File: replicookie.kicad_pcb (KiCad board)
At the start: 4 copper layers, 152.4 x 114.3 mm, 160 parts, among them J1001 Conn_01x08_Female, J1002 Screw_Terminal_01x04, J1003 Conn_02x03_Odd_Even, J1004 Conn_01x08_Female, J1101 Conn_01x08_Female, J1102 Screw_Terminal_01x04, J1103 Conn_02x03_Odd_Even, J1104 Conn_01x08_Female, J1201 Conn_01x08_Female, J1202 Screw_Terminal_01x04, J1203 Conn_02x03_Odd_Even, J1204 Conn_01x08_Female, J1301 Conn_01x08_Female, J1302 Screw_Terminal_01x04, J1303 Conn_02x03_Odd_Even, J1304 Conn_01x08_Female, J1401 Conn_01x08_Female, J1402 Screw_Terminal_01x04, J1403 Conn_02x03_Odd_Even, J1404 Conn_01x08_Female, J1501 Conn_01x08_Female, J1502 Screw_Terminal_01x04, J1503 Conn_02x03_Odd_Even, J1504 Conn_01x08_Female, J301 USB_B_Micro, J401 JK0654219, J501 USB_A, J502 USB_A, J801 Conn_01x08_Female, J802 Screw_Terminal_01x04, J803 Conn_02x03_Odd_Even, J804 Conn_01x08_Female, J901 Conn_01x08_Female, J902 Screw_Terminal_01x04, J903 Conn_02x03_Odd_Even, J904 Conn_01x08_Female, P601 TFM-115-01-F-D-A, P602 TFM-120-01-F-D-A, U201 DS1307ZN+, U301 93LCxxBxxOT, U302 FT2232HQ, U401 MIC33050-4YHL, U402 TXS0102DCU, U403 KSZ9031RNXCA, U404 ASDMB-25.000MHz, U405 74LVC2G07, U501 ASDMB-24.000MHz-C, U502 ASDMB-26.000MHz-C, U503 USB3343, U504 74LVC1G07, U505 USB2514B_Bi, X201 ASE-xxxMHz, Y301 ABM8-12.000MHZ-20

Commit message: Connect Ethernet PHY to FPGA, route RGMII signals
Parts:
- removed the C402 at (113.0, 46.9)
- removed the C404 at (113.0, 48.9)
- removed the U402 at (144.8, 90.2)
- added C601: 0.1u, Capacitor_SMD:C_0603_1608Metric, F.Cu at (251.0, 116.3)
- added C602: 0.1u, Capacitor_SMD:C_0603_1608Metric, F.Cu at (255.0, 116.3)
- added U601: TCA9800, Package_SO:VSSOP-8_3.0x3.0mm_P0.65mm, F.Cu at (257.8, 106.0)
- C401: footprint Capacitor_SMD:C_0402_1005Metric -> Capacitor_SMD:C_0603_1608Metric; moved to F.Cu
- C402: renamed from C403; footprint Capacitor_SMD:C_0402_1005Metric -> Capacitor_SMD:C_0603_1608Metric; moved to F.Cu
- C403: renamed from C405; moved to F.Cu
- C408: renamed from C410; value 0.1U -> 0.1u; moved to B.Cu
- C409: renamed from C411; value 0.1U -> 0.1u; moved to B.Cu
- C410: renamed from C412; value 0.1U -> 0.1u
- C411: renamed from C413; value 0.1U -> 0.1u
- C412: renamed from C414; value 0.1U -> 0.1u
- C413: renamed from C415; value 0.1U -> 0.1u; moved to B.Cu
- C414: renamed from C416; value 0.1U -> 0.1u; moved to B.Cu
- C415: renamed from C417; value 0.1U -> 0.1u
- C416: renamed from C418; value 0.1U -> 0.1u; moved to B.Cu
- C417: renamed from C419; value 0.1U -> 0.1u
- C418: renamed from C420; value 0.1U -> 0.1u; moved to B.Cu
- C419: renamed from C421; value 0.1U -> 0.1u; moved to B.Cu
- C420: renamed from C422; value 0.1U -> 0.1u; moved to B.Cu
- C421: renamed from C423; value 0.1U -> 0.1u
- C422: renamed from C424; footprint Capacitor_SMD:C_0402_1005Metric -> Capacitor_SMD:C_0603_1608Metric
- C423: renamed from C425; footprint Capacitor_SMD:C_0402_1005Metric -> Capacitor_SMD:C_0603_1608Metric
- C425: renamed from C427; footprint Capacitor_SMD:C_0402_1005Metric -> Capacitor_SMD:C_0603_1608Metric
- C426: renamed from C428; footprint Capacitor_SMD:C_0402_1005Metric -> Capacitor_SMD:C_0603_1608Metric
- C427: renamed from C429; footprint Capacitor_SMD:C_0402_1005Metric -> Capacitor_SMD:C_0603_1608Metric
- C428: renamed from C430; footprint Capacitor_SMD:C_0402_1005Metric -> Capacitor_SMD:C_0603_1608Metric
- R403, R405: footprint Resistor_SMD:R_0603_1608Metric -> Resistor_SMD:R_0402_1005Metric; moved to B.Cu
- U401: moved to F.Cu
- U404: renamed from U405; moved to B.Cu
- moved C423 216.6 mm to (275.3, 124.7), turned to 180 degrees
- moved D401 199.6 mm to (272.2, 119.8), turned to -90 degrees
- moved R407 198.4 mm to (278.0, 127.1)
- moved D402 198.0 mm to (275.3, 126.6)
- moved U404 195.1 mm to (260.8, 124.3), turned to 90 degrees
- moved R403 181.4 mm to (255.9, 128.4), turned to 180 degrees
- moved R405 180.0 mm to (255.9, 126.7), turned to 180 degrees
- moved C403 175.9 mm to (284.5, 124.5), turned to -90 degrees
- moved C404 175.6 mm to (292.2, 133.8)
- moved C406 175.6 mm to (292.2, 135.7)
- moved C407 175.6 mm to (292.2, 137.6)
- moved C424 175.6 mm to (292.2, 139.5)
- moved FB401 175.6 mm to (288.4, 135.7)
- moved FB402 175.6 mm to (288.4, 137.6)
- moved FB403 175.6 mm to (288.4, 139.5)
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- renumbered C406 to C404, C407 to C405, C408 to C406, C409 to C407, C426 to C424, P601 to J2, P602 to J3, PA601 to JA1, PA602 to JA2, PB601 to JB1, PB602 to JB2, PC601 to JC1, U403 to U402, U404 to U403
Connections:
- net /Snickerdoodle/~ETHERNET_RST renamed Net-(J3-Pad2)
- net /Snickerdoodle/~USB_RST renamed Net-(J3-Pad4)
- net /ZYNQ_I2C1.SCL renamed /SMB_I2C1.SCL
- net /ZYNQ_I2C1.SDA renamed /SMB_I2C1.SDA
- net /ZYNQ_I2C2.SCL renamed /SMB_I2C2.SCL
- net /ZYNQ_I2C2.SDA renamed /SMB_I2C2.SDA
- net /ZYNQ_I2C3.SCL renamed /SMB_I2C3.SCL
- net /ZYNQ_I2C3.SDA renamed /SMB_I2C3.SDA
- net /ZYNQ_I2C4.SCL renamed /SMB_I2C4.SCL
- net /ZYNQ_I2C4.SDA renamed /SMB_I2C4.SDA
- net /ZYNQ_I2C5.SCL renamed /SMB_I2C5.SCL
- net /ZYNQ_I2C5.SDA renamed /SMB_I2C5.SDA
- net /ZYNQ_I2C7.SCL renamed /SMB_I2C7.SCL
- net /ZYNQ_I2C7.SDA renamed /SMB_I2C7.SDA
- net /~RESET renamed /~USB_RST
- net Net-(C327-Pad1) renamed /Ethernet/CT4
- net Net-(C328-Pad1) renamed /Ethernet/CT3
- net Net-(C329-Pad1) renamed /Ethernet/CT2
- net Net-(C330-Pad1) renamed /Ethernet/CT1
- net Net-(J301-Pad14) renamed /Ethernet/LED2A
- net Net-(J301-Pad16) renamed /Ethernet/LED1A
- net Net-(R301-Pad2) renamed /Ethernet/LED_MODE
- net Net-(R306-Pad1) renamed /Ethernet/ISET
- C405 pad 1: +1V8 -> +3V3
- C408 pad 1: +1V8 -> +3V3
- C409 pad 1: +1V8 -> +3V3
- C410 pad 1: +1V8 -> +3V3
- D401 pad 1: +1V8 -> +3V3
- D402 pad 1: /~RESET_1 -> /~ETHERNET_RST
- J3 pad 11: /ETHERNET.TXD3 -> Net-(J3-Pad11)
- J3 pad 12: /ETHERNET.RXD0 -> Net-(J3-Pad12)
- J3 pad 13: /ETHERNET.TX_CTL -> Net-(J3-Pad13)
- J3 pad 14: /ETHERNET.RX_CLK -> Net-(J3-Pad14)
- J3 pad 17: /ETHERNET.RXD1 -> Net-(J3-Pad17)
- J3 pad 18: /ETHERNET.RX_CTL -> Net-(J3-Pad18)
- J3 pad 19: /ETHERNET.RXD2 -> Net-(J3-Pad19)
- J3 pad 20: /ETHERNET.RXD3 -> Net-(J3-Pad20)
- J3 pad 5: /ETHERNET.TX_CLK -> Net-(J3-Pad5)
- J3 pad 6: /ETHERNET.TXD2 -> /Snickerdoodle/SCK
- J3 pad 7: /ETHERNET.TXD0 -> Net-(J3-Pad7)
- J3 pad 8: /ETHERNET.TXD1 -> /Snickerdoodle/SCL
- JA2 pad 12: Net-(PA502-Pad12) -> /ETHERNET.TXD3
- JA2 pad 14: Net-(PA502-Pad14) -> /ETHERNET.TX_CLK
- JA2 pad 17: Net-(PA502-Pad17) -> /ETHERNET.MDIO
- JA2 pad 18: Net-(PA502-Pad18) -> /ETHERNET.TX_CTL
- JA2 pad 19: Net-(PA502-Pad19) -> /ETHERNET.MDC
- JA2 pad 20: Net-(PA502-Pad20) -> /ETHERNET.RXD3
- JA2 pad 24: Net-(PA502-Pad24) -> /ETHERNET.RXD2
- JA2 pad 26: Net-(PA502-Pad26) -> /ETHERNET.RXD1
- JA2 pad 30: Net-(PA502-Pad30) -> /ETHERNET.RXD0
- JA2 pad 32: Net-(PA502-Pad32) -> /ETHERNET.RX_CTL
- JA2 pad 36: /ETHERNET.MDC -> /ETHERNET.RX_CLK
- JA2 pad 38: /ETHERNET.MDIO -> /~ETHERNET_RST
- JA2 pad 4: Net-(PA502-Pad4) -> /ETHERNET.TXD0
- JA2 pad 6: Net-(PA502-Pad6) -> /ETHERNET.TXD1
- JA2 pad 8: Net-(PA502-Pad8) -> /ETHERNET.TXD2
- R401 pad 1: +1V8 -> +3V3
- R402 pad 1: +1V8 -> +3V3
- R402 pad 2: /Ethernet/LED2 -> /Ethernet/~INT~/~PME2
- R404 pad 1: +1V8 -> +3V3
- R404 pad 2: /Ethernet/MDIO -> /ETHERNET.MDIO
- R407 pad 1: +1V8 -> +3V3
- U402 pad 16: +1V8 -> +3V3
- U402 pad 34: +1V8 -> +3V3
- U402 pad 36: /Ethernet/MDC -> /ETHERNET.MDC
- U402 pad 37: /Ethernet/MDIO -> /ETHERNET.MDIO
- U402 pad 38: /Ethernet/LED2 -> /Ethernet/~INT~/~PME2
- U402 pad 40: +1V8 -> +3V3
- U404 pad 1: /Ethernet/LED1 -> /Ethernet/LED2
- U404 pad 3: /Ethernet/LED2 -> /Ethernet/LED1
- U404 pad 4: /Ethernet/LED2K -> /Ethernet/LED1K
- U404 pad 5: +1V8 -> +3V3
- U404 pad 6: /Ethernet/LED1K -> /Ethernet/LED2K
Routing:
- net /ETHERNET.TX_CTL: track 0.00 -> 42.0 mm
- net /ETHERNET.TXD3: track 0.00 -> 42.0 mm
- net /ETHERNET.TX_CLK: track 0.00 -> 41.9 mm
- net /ETHERNET.TXD0: track 0.00 -> 41.9 mm
- net /ETHERNET.TXD1: track 0.00 -> 41.8 mm
- net /ETHERNET.TXD2: track 0.00 -> 41.7 mm
- net /ETHERNET.RX_CLK: track 0.00 -> 33.2 mm
- net /ETHERNET.RXD1: track 0.00 -> 33.1 mm
- net /ETHERNET.RX_CTL: track 0.00 -> 33.0 mm
- net /ETHERNET.RXD2: track 0.00 -> 33.0 mm
- net /ETHERNET.RXD3: track 0.00 -> 32.7 mm
- net /ETHERNET.RXD0: track 0.00 -> 32.5 mm
- net GND: track 0.00 -> 23.7 mm, vias 0 -> 4
- net /Ethernet/LED1: track 0.00 -> 9.27 mm, vias 0 -> 1
- net /Ethernet/DVDDL: track 16.8 -> 24.7 mm, vias 0 -> 6
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- added copper zone on In2.Cu, net +3V3
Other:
- board size 152.4 x 114.3 mm -> 160 x 120 mm

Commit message: Attach ethernet to PL, layout and route
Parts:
- added C429: 0.1u, Capacitor_SMD:C_0603_1608Metric, F.Cu at (260.2, 121.0)
- C401, C403, C404, C405, C406, C407, C415, C421, U401: moved to B.Cu
- C402: footprint Capacitor_SMD:C_0603_1608Metric -> Capacitor_SMD:C_0402_1005Metric; moved to B.Cu
- D401, D402: value 1N4148WS -> 1N4148WT; footprint Diode_SMD:D_SOD-323 -> Diode_SMD:D_SOD-523
- FB301, FB302: footprint Inductor_SMD:L_0603_1608Metric -> Inductor_SMD:L_0402_1005Metric
- FB401, FB402, FB403: footprint Inductor_SMD:L_0603_1608Metric -> Inductor_SMD:L_0402_1005Metric; moved to B.Cu
- R401: footprint Resistor_SMD:R_0603_1608Metric -> Resistor_SMD:R_0402_1005Metric; moved to B.Cu
- R402, R404, R406: footprint Resistor_SMD:R_0603_1608Metric -> Resistor_SMD:R_0402_1005Metric
- R403, R405, U404: moved to F.Cu
- U302: value FT2232HQ -> FT4232H; footprint Package_DFN_QFN:QFN-64-1EP_9x9mm_P0.5mm_EP4.35x4.35mm -> Package_QFP:LQFP-64_10x10mm_P0.5mm
- moved C427 110.8 mm to (285.0, 115.0), turned to -90 degrees
- moved R404 101.4 mm to (279.5, 134.8), turned to 180 degrees
- moved U302 89.8 mm to (158.5, 91.2)
- moved R408 78.1 mm to (269.5, 115.0), turned to -90 degrees
- moved C422 75.8 mm to (282.5, 125.0), turned to 180 degrees
- moved C425 74.1 mm to (263.5, 115.0), turned to -90 degrees
- moved U403 72.6 mm to (282.5, 128.0), turned to 180 degrees
- moved R402 69.6 mm to (279.5, 133.5), turned to 180 degrees
- moved R401 66.1 mm to (278.8, 131.5), turned to 180 degrees
- moved R406 65.7 mm to (279.0, 128.0)
- moved R409 59.3 mm to (280.0, 115.0), turned to -90 degrees
- moved C428 59.0 mm to (282.5, 115.0), turned to -90 degrees
- moved C426 42.5 mm to (261.0, 115.0), turned to -90 degrees
- moved U401 41.8 mm to (287.7, 134.8), turned to 180 degrees
- moved C424 28.1 mm to (268.0, 125.2), turned to 90 degrees
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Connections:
- net /Ethernet/~RESET_IN renamed /Ethernet/~ENET_RST
- net /SCL renamed /SMB_I2C0.SCL
- net /SDA renamed /SMB_I2C0.SDA
- net Net-(U504-Pad4) renamed /USB/~HUB_RESET
- C422 pad 2: Net-(C422-Pad2) -> GND
- J401 pad 4: /Ethernet/TXRXB+ -> /Ethernet/TXRXB-
- J401 pad 5: /Ethernet/TXRXB- -> /Ethernet/TXRXB+
- J401 pad 8: /Ethernet/TXRXD+ -> /Ethernet/TXRXD-
- J401 pad 9: /Ethernet/TXRXD- -> /Ethernet/TXRXD+
- JA2 pad 17: /ETHERNET.MDIO -> Net-(JA2-Pad17)
- JA2 pad 19: /ETHERNET.MDC -> Net-(JA2-Pad19)
- JA2 pad 31: Net-(JA2-Pad31) -> /~ETHERNET_RST
- JA2 pad 35: Net-(JA2-Pad35) -> /ETHERNET.MDIO
- JA2 pad 37: Net-(JA2-Pad37) -> /ETHERNET.MDC
- JA2 pad 38: /~ETHERNET_RST -> Net-(JA2-Pad38)
- U403 pad 2: Net-(C422-Pad2) -> GND
- U404 pad 1: /Ethernet/LED2 -> /Ethernet/LED1
- U404 pad 3: /Ethernet/LED1 -> /Ethernet/LED2
- U404 pad 4: /Ethernet/LED1K -> /Ethernet/LED2K
- U404 pad 6: /Ethernet/LED2K -> /Ethernet/LED1K
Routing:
- net /~ETHERNET_RST: track 0.00 -> 42.3 mm
- net /ETHERNET.MDIO: track 0.00 -> 38.5 mm
- net /ETHERNET.MDC: track 0.00 -> 35.6 mm
- net +3V3: track 7.11 -> 30.8 mm, vias 3 -> 11
- net /Ethernet/TXRXB+: track 0.00 -> 23.4 mm
- net /Ethernet/TXRXC-: track 0.00 -> 23.4 mm
- net /Ethernet/TXRXB-: track 0.00 -> 22.6 mm
- net /Ethernet/TXRXC+: track 0.00 -> 22.6 mm
- net /Ethernet/TXRXA+: track 0.00 -> 20.6 mm
- net /Ethernet/TXRXD-: track 0.00 -> 20.6 mm
- net /Ethernet/TXRXA-: track 0.00 -> 19.9 mm
- net /Ethernet/TXRXD+: track 0.00 -> 19.9 mm
- net /Ethernet/LED1K: track 0.00 -> 19.9 mm, vias 0 -> 1
- net /Ethernet/CT2: track 0.00 -> 12.7 mm
- net /Ethernet/CT3: track 0.00 -> 12.5 mm
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- added copper zone on B.Cu, net +3V3
- added copper zone on B.Cu, net /Ethernet/DVDDL
- added copper zone on In2.Cu, net /Ethernet/DVDDL
- added copper zone on B.Cu, net Net-(U401-Pad3)

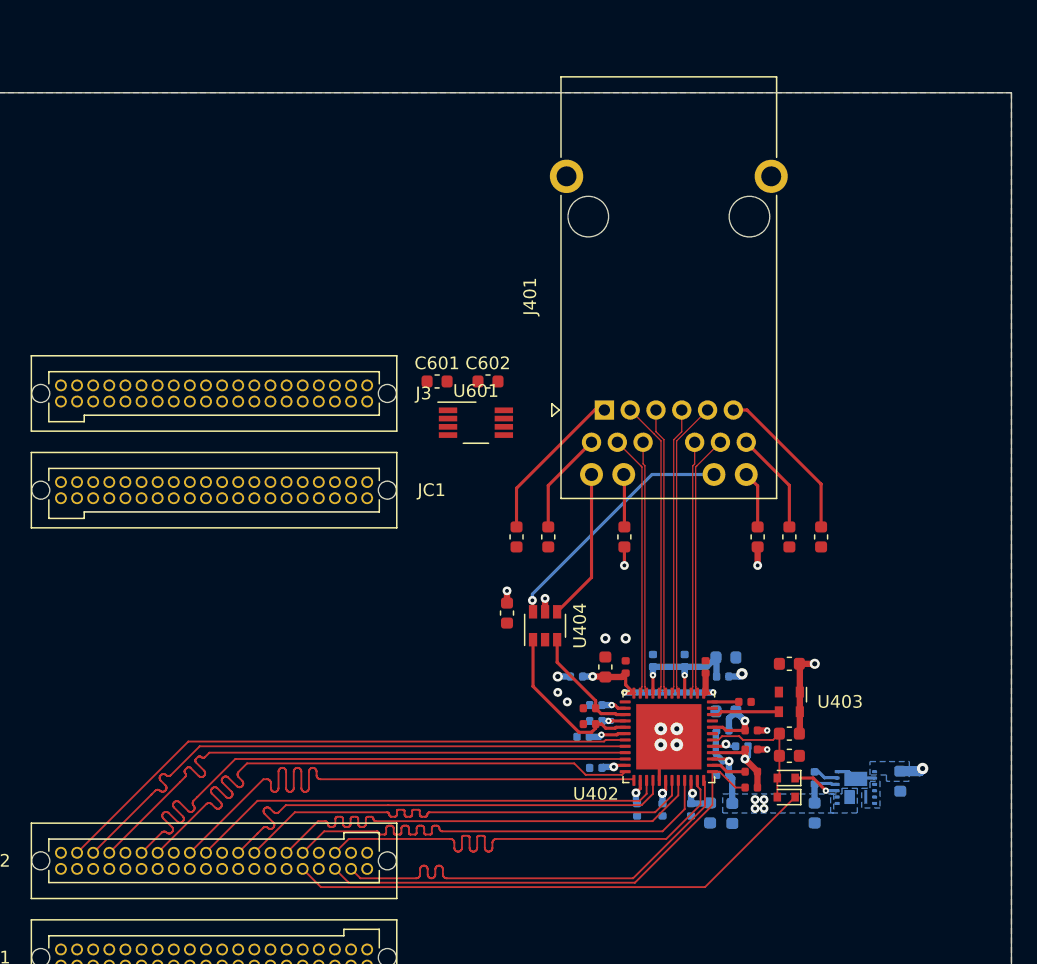
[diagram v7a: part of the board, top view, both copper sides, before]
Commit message: Move Ethernet around to save space
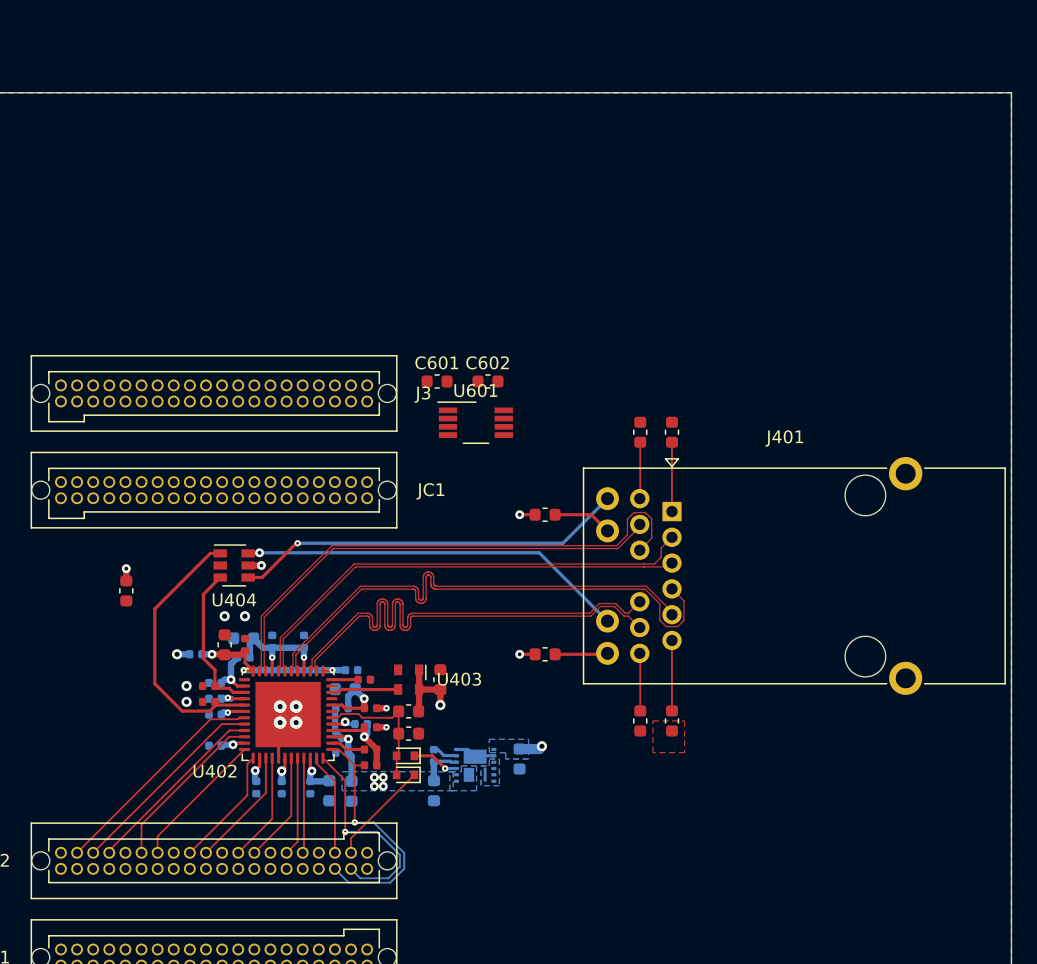
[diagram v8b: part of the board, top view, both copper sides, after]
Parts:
- C411: moved to B.Cu
- moved C406 38.0 mm to (239.5, 123.0), turned to 180 degrees
- moved FB401 37.8 mm to (239.5, 124.5), turned to 180 degrees
- moved C412 30.1 mm to (239.6, 123.5)
- moved FB403 30.1 mm to (235.7, 124.2)
- moved C401 30.1 mm to (261.2, 132.5)
- moved C402 30.1 mm to (254.5, 132.2)
- moved C403 30.1 mm to (254.5, 135.0)
- moved C404 30.1 mm to (248.0, 135.0)
- moved C405 30.1 mm to (246.2, 135.0)
- moved C407 30.1 mm to (247.5, 127.0)
- moved C408 30.1 mm to (237.2, 127.8)
- moved C409 30.1 mm to (244.8, 134.8)
- moved C410 30.1 mm to (249.5, 130.0)
- moved C413 30.1 mm to (237.2, 126.5)
- moved C417 30.1 mm to (249.5, 128.5)
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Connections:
- J401 pad 4: /Ethernet/TXRXB- -> /Ethernet/TXRXB+
- J401 pad 5: /Ethernet/TXRXB+ -> /Ethernet/TXRXB-
- J401 pad 8: /Ethernet/TXRXD- -> /Ethernet/TXRXD+
- J401 pad 9: /Ethernet/TXRXD+ -> /Ethernet/TXRXD-
- JA2 pad 31: /~ETHERNET_RST -> Net-(JA2-Pad31)
- JA2 pad 38: Net-(JA2-Pad38) -> /~ETHERNET_RST
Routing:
- net /ETHERNET.TX_CTL: track 47.0 -> 9.52 mm
- net /ETHERNET.TX_CLK: track 46.9 -> 11.0 mm
- net /~ETHERNET_RST: track 42.3 -> 8.21 mm
- net /ETHERNET.TXD3: track 47.0 -> 13.2 mm
- net /ETHERNET.TXD2: track 46.7 -> 14.7 mm
- net /ETHERNET.TXD1: track 46.9 -> 16.1 mm
- net /ETHERNET.RX_CTL: track 38.0 -> 7.49 mm
- net /ETHERNET.RX_CLK: track 38.1 -> 8.05 mm
- net /ETHERNET.RXD0: track 37.5 -> 7.81 mm
- net /ETHERNET.RXD2: track 38.0 -> 8.56 mm
- net /ETHERNET.RXD1: track 38.1 -> 8.66 mm
- net /ETHERNET.TXD0: track 46.9 -> 17.6 mm
- net /ETHERNET.RXD3: track 37.7 -> 9.41 mm
- net /Ethernet/TXRXD-: track 20.6 -> 42.3 mm
- net /Ethernet/TXRXB+: track 23.4 -> 42.8 mm
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- added copper zone on F.Cu, net (none)
